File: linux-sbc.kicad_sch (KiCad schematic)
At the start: 9 parts, among them J101 Molex Mini-fit Jr

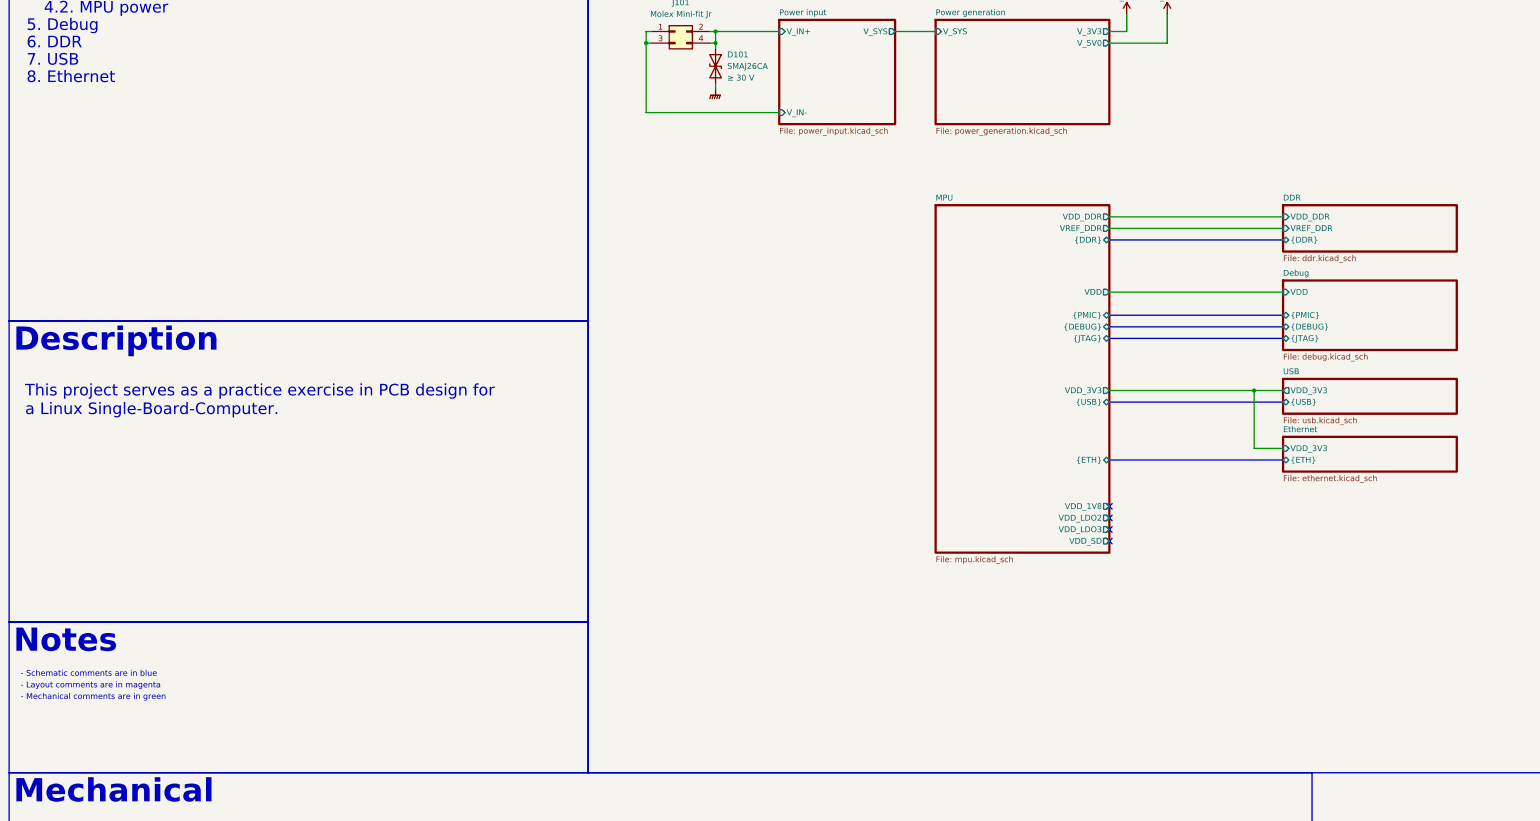
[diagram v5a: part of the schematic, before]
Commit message: Add microSD card
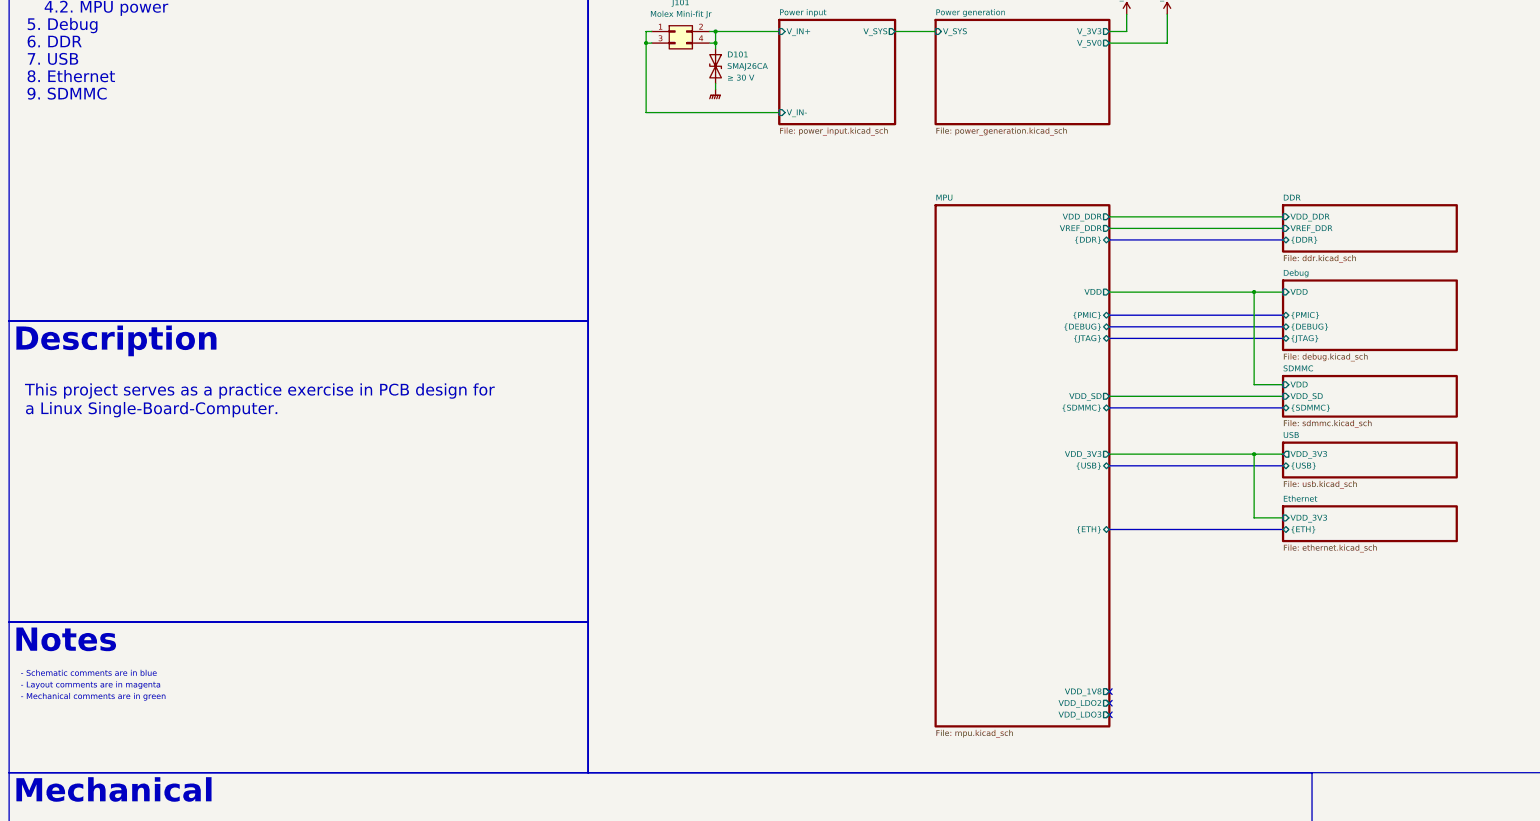
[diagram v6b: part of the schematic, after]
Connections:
- no-connect marks 4 -> 3
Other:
- added sheet SDMMC (sdmmc.kicad_sch)
- sheet MPU ports: added {SDMMC}; removed none
- note added: "9. SDMMC"
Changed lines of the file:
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@@
 		(rev "v0.0.1")
+	)
+	(bus_alias "SDMMC"
+		(members "SDMMC.D[0..3]" "SDMMC.CMD" "SDMMC.CLK" "SDMMC.DET_N")
 	)
 	(text "7. USB"
@@
 		)
 	)
+	(text "9. SDMMC"
+		(exclude_from_sim no)
+		(at 16.51 102.87 0)
+		(effects
+			(font
+				(size 2.54 2.54)
+			)
+			(justify left)
+			(href "#11")
+		)
+	)
 	(text "Place a stitched chassis guard rail along the edges of the PCB\nto provide a safe point for human contact when handling the device."
 		(exclude_from_sim no)
@@
 	)
 	(junction
+		(at 285.75 146.05)
+		(diameter 0)
+		(color 0 0 0 0)
+	)
+	(junction
 		(at 38.1 279.4)
 		(diameter 0)
@@
 	)
 	(junction
-		(at 285.75 167.64)
+		(at 285.75 181.61)
 		(diameter 0)
 		(color 0 0 0 0)
@@
 	)
 	(no_connect
-		(at 254 198.12)
+		(at 254 238.76)
 	)
 	(no_connect
-		(at 254 200.66)
+		(at 254 233.68)
 	)
 	(no_connect
-		(at 254 193.04)
-	)
-	(no_connect
-		(at 254 195.58)
+		(at 254 236.22)
 	)
 	(wire
@@
 	(wire
 		(pts
-			(xy 285.75 167.64) (xy 292.1 167.64)
+			(xy 285.75 181.61) (xy 292.1 181.61)
 		)
 		(stroke
@@
 	(wire
 		(pts
+			(xy 285.75 146.05) (xy 292.1 146.05)
+		)
+		(stroke
+			(width 0)
+			(type default)
+		)
+	)
+	(wire
+		(pts
 			(xy 153.67 88.9) (xy 152.4 88.9)
 		)
@@
 	(bus
 		(pts
-			(xy 254 170.18) (xy 292.1 170.18)
+			(xy 254 184.15) (xy 292.1 184.15)
 		)
 		(stroke
@@
 	(wire
 		(pts
+			(xy 292.1 166.37) (xy 285.75 166.37)
+		)
+		(stroke
+			(width 0)
+			(type default)
+		)
+	)
+	(wire
+		(pts
 			(xy 29.21 279.4) (xy 38.1 279.4)
 		)
@@
 	(bus
 		(pts
-			(xy 254 182.88) (xy 292.1 182.88)
-		)
-		(stroke
-			(width 0)
-			(type default)
-		)
-	)
-	(wire
-		(pts
-			(xy 285.75 180.34) (xy 292.1 180.34)
+			(xy 254 198.12) (xy 292.1 198.12)
+		)
+		(stroke
+			(width 0)
+			(type default)
+		)
+	)
+	(wire
+		(pts
+			(xy 285.75 195.58) (xy 292.1 195.58)
 		)
 		(stroke
@@
 	(wire
 		(pts
+			(xy 285.75 166.37) (xy 285.75 146.05)
+		)
+		(stroke
+			(width 0)
+			(type default)
+		)
+	)
+	(wire
+		(pts
 			(xy 152.4 88.9) (xy 152.4 91.44)
 		)
@@
 	(wire
 		(pts
-			(xy 254 167.64) (xy 285.75 167.64)
+			(xy 254 181.61) (xy 285.75 181.61)
 		)
 		(stroke
@@
 	(wire
 		(pts
+			(xy 254 168.91) (xy 292.1 168.91)
+		)
+		(stroke
+			(width 0)
+			(type default)
+		)
+	)
+	(wire
+		(pts
 			(xy 57.15 278.13) (xy 57.15 279.4)
 		)
@@
 	(wire
 		(pts
-			(xy 285.75 167.64) (xy 285.75 180.34)
+			(xy 285.75 181.61) (xy 285.75 195.58)
 		)
 		(stroke
@@
 		)
 	)
+	(bus
+		(pts
+			(xy 254 171.45) (xy 292.1 171.45)
+		)
+		(stroke
+			(width 0)
+			(type default)
+		)
+	)
 	(wire
 		(pts
@@
 	(wire
 		(pts
-			(xy 254 146.05) (xy 292.1 146.05)
+			(xy 254 146.05) (xy 285.75 146.05)
 		)
 		(stroke
@@
 	)
 	(sheet
-		(at 215.9 127)
-		(size 38.1 76.2)
+		(at 292.1 164.465)
+		(size 38.1 8.89)
 		(exclude_from_sim no)
 		(in_bom yes)
@@
 			(color 0 255 0 1.0000)
 		)
+		(property "Sheetname" "SDMMC"
+			(at 292.1 163.5796 0)
+			(effects
+				(font
+					(size 1.27 1.27)
+				)
+				(justify left bottom)
+			)
+		)
+		(property "Sheetfile" "sdmmc.kicad_sch"
+			(at 292.1 174.1134 0)
+			(effects
+				(font
+					(size 1.27 1.27)
+				)
+				(justify left top)
+			)
+		)
+		(pin "VDD_SD" input
+			(at 292.1 168.91 180)
+			(effects
+				(font
+					(size 1.27 1.27)
+				)
+				(justify left)
+			)
+		)
+		(pin "VDD" input
+			(at 292.1 166.37 180)
+			(effects
+				(font
+					(size 1.27 1.27)
+				)
+				(justify left)
+			)
+		)
+		(pin "{SDMMC}" bidirectional
+			(at 292.1 171.45 180)
+			(effects
+				(font
+					(size 1.27 1.27)
+				)
+				(justify left)
+			)
+		)
+		(instances
+			(project "linux-sbc"
+				(path "/fa11a02f-8043-4153-ab69-88d766503017"
+					(page "11")
+				)
+			)
+		)
+	)
+	(sheet
+		(at 215.9 127)
+		(size 38.1 114.3)
+		(exclude_from_sim no)
+		(in_bom yes)
+		(on_board yes)
+		(dnp no)
+		(fields_autoplaced yes)
+		(stroke
+			(width 0.5)
+			(type solid)
+			(color 255 255 0 1)
+		)
+		(fill
+			(color 0 255 0 1.0000)
+		)
 		(property "Sheetname" "MPU"
 			(at 215.9 126.1146 0)
@@
 		)
 		(property "Sheetfile" "mpu.kicad_sch"
-			(at 215.9 203.9584 0)
+			(at 215.9 242.0584 0)
 			(effects
 				(font
@@
 		)
 		(pin "{USB}" bidirectional
-			(at 254 170.18 0)
+			(at 254 184.15 0)
 			(effects
 				(font
@@
 		)
 		(pin "VDD_1V8" output
-			(at 254 193.04 0)
+			(at 254 233.68 0)
 			(effects
 				(font
@@
 		)
 		(pin "VDD_3V3" output
-			(at 254 167.64 0)
+			(at 254 181.61 0)
 			(effects
 				(font
@@
 		)
 		(pin "VDD_LDO2" output
-			(at 254 195.58 0)
+			(at 254 236.22 0)
 			(effects
 				(font
@@
 		)
 		(pin "VDD_LDO3" output
-			(at 254 198.12 0)
+			(at 254 238.76 0)
 			(effects
 				(font
@@
 		)
 		(pin "VDD_SD" output
-			(at 254 200.66 0)
+			(at 254 168.91 0)
 			(effects
 				(font
@@
 		)
 		(pin "{ETH}" bidirectional
-			(at 254 182.88 0)
+			(at 254 198.12 0)
+			(effects
+				(font
+					(size 1.27 1.27)
+				)
+				(justify right)
+			)
+		)
+		(pin "{SDMMC}" bidirectional
+			(at 254 171.45 0)
 			(effects
 				(font
@@
 	)
 	(sheet
-		(at 292.1 177.8)
+		(at 292.1 193.04)
 		(size 38.1 7.62)
 		(exclude_from_sim no)
@@
 		)
 		(property "Sheetname" "Ethernet"
-			(at 292.1 176.9146 0)
+			(at 292.1 192.1546 0)
 			(effects
 				(font
@@
 		)
 		(property "Sheetfile" "ethernet.kicad_sch"
-			(at 292.1 186.1784 0)
+			(at 292.1 201.4184 0)
 			(effects
 				(font
@@
 		)
 		(pin "VDD_3V3" input
-			(at 292.1 180.34 180)
+			(at 292.1 195.58 180)
 			(effects
 				(font
@@
 		)
 		(pin "{ETH}" bidirectional
-			(at 292.1 182.88 180)
+			(at 292.1 198.12 180)
 			(effects
 				(font
@@
 	)
 	(sheet
-		(at 292.1 165.1)
+		(at 292.1 179.07)
 		(size 38.1 7.62)
 		(exclude_from_sim no)
@@
 		)
 		(property "Sheetname" "USB"
-			(at 292.1 164.2146 0)
+			(at 292.1 178.1846 0)
 			(effects
 				(font
@@
 		)
 		(property "Sheetfile" "usb.kicad_sch"
-			(at 292.1 173.4784 0)
+			(at 292.1 187.4484 0)
 			(effects
 				(font
@@
 		)
 		(pin "{USB}" bidirectional
-			(at 292.1 170.18 180)
+			(at 292.1 184.15 180)
 			(effects
 				(font
@@
 		)
 		(pin "VDD_3V3" output
-			(at 292.1 167.64 180)
-			(effects
-				(font
+			(at 292.1 181.61 180)
+			(effects
+				(font

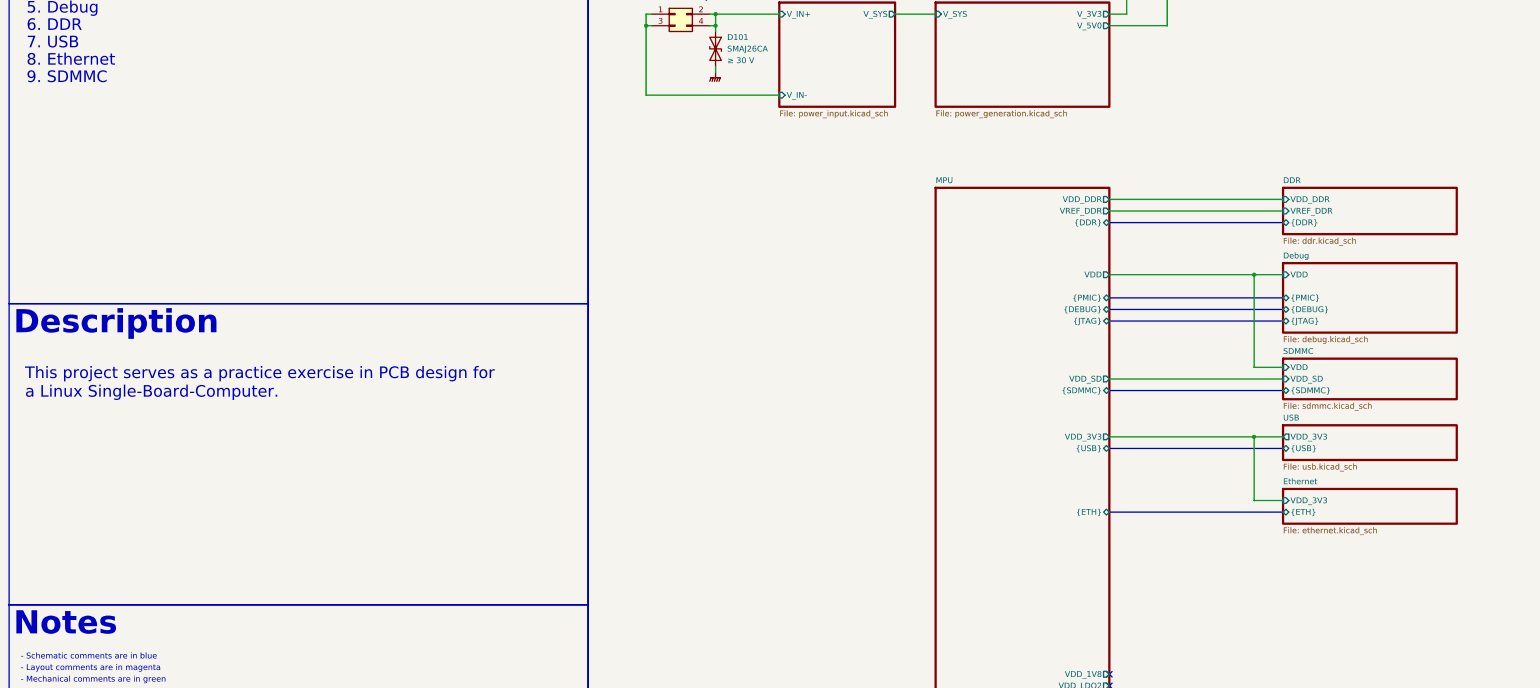
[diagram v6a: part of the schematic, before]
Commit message: Add keypad
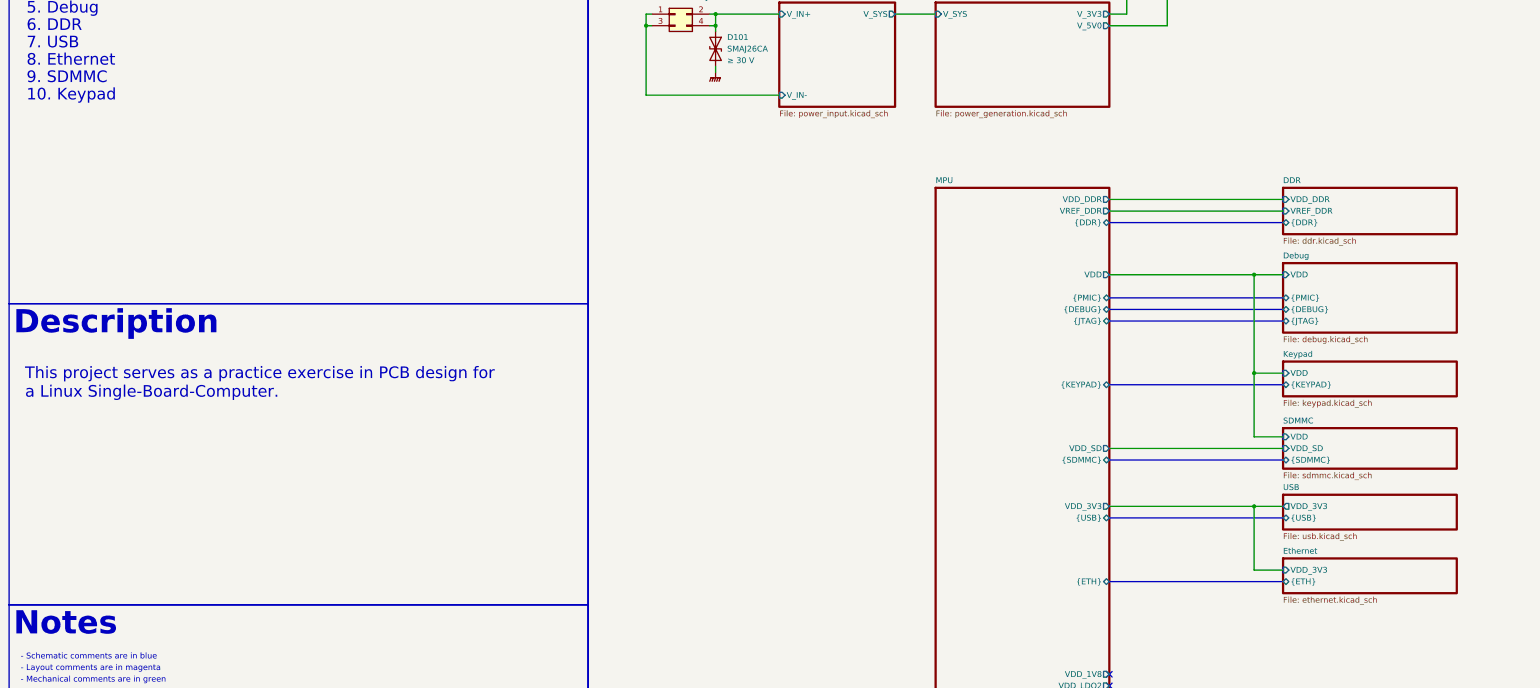
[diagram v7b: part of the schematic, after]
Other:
- added sheet Keypad (keypad.kicad_sch)
- sheet MPU ports: added {KEYPAD}; removed none
- note added: "10. Keypad"

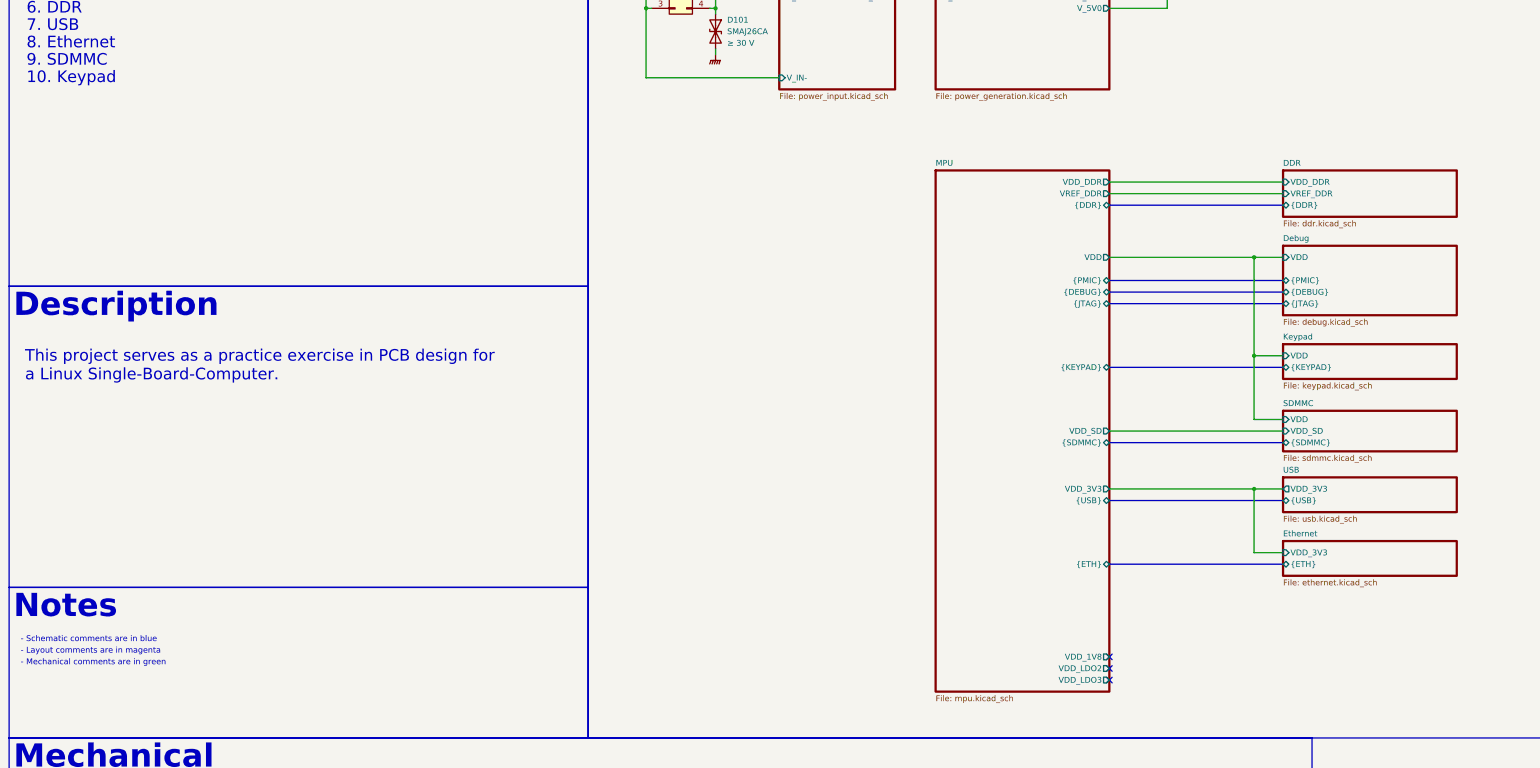
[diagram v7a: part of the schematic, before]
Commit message: Add wireless schema
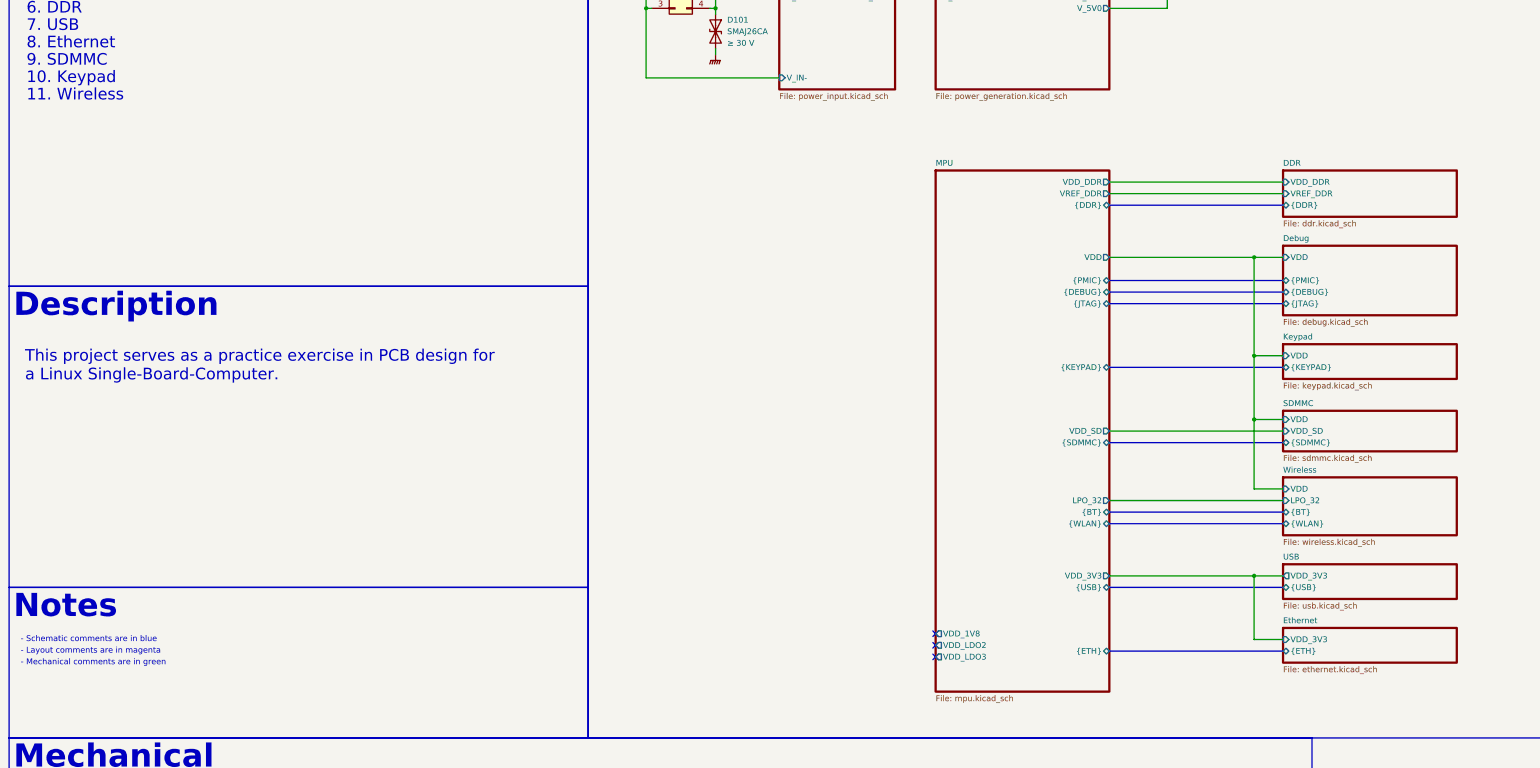
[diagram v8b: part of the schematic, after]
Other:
- added sheet Wireless (wireless.kicad_sch)
- sheet MPU ports: added LPO_32, {BT}, {WLAN}; removed none
- note added: "11. Wireless"
